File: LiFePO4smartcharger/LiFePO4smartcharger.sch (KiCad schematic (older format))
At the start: 106 parts, among them J1 Conn_01x02, J10 Conn_01x01, J11 Conn_01x01, J12 Conn_01x04, J14 Conn_01x02, J2 Conn_02x03_Odd_Even, J3 Conn_01x02, J4 Conn_01x02, J5 Conn_01x02, J6 Conn_01x01, J7 Conn_01x01, J8 Conn_01x02, J9 Conn_01x02, Q1 TIP42, Q2 TIP41, Q3 2N3906, Q4 TIP41C, U1 ATMEGA328P-PU, U2 LM358, U3 LCD-016N002L, U4 TL494, U5 LMT85, U9 LM7805_TO220, X3 16MHz

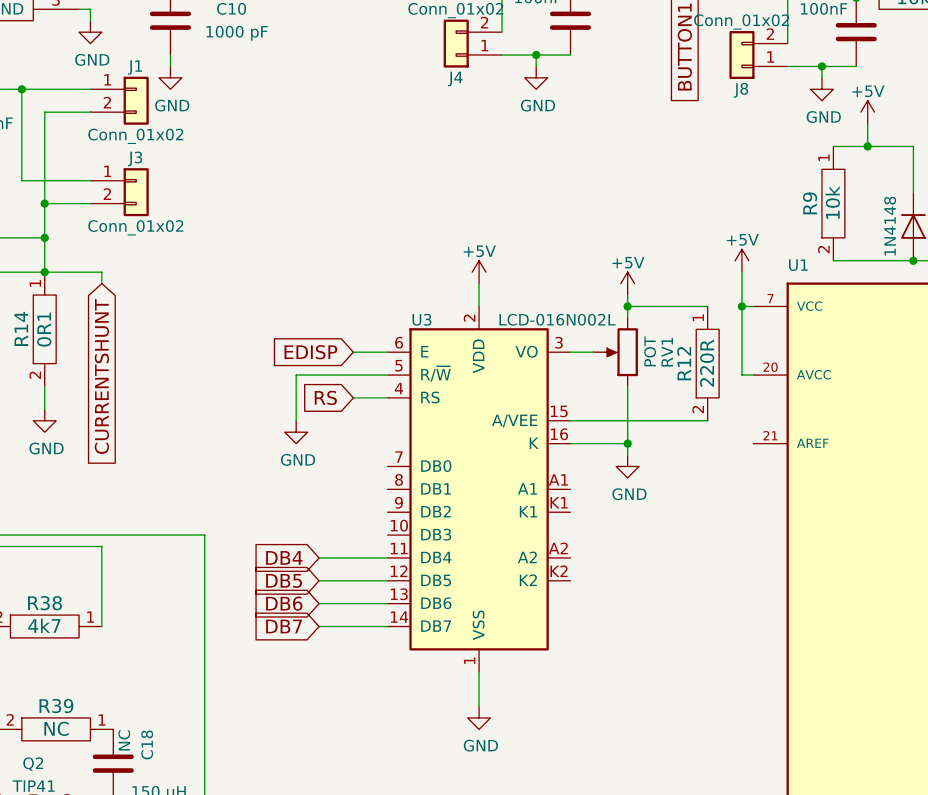
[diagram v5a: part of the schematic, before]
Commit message: Changed temperature sensor interface
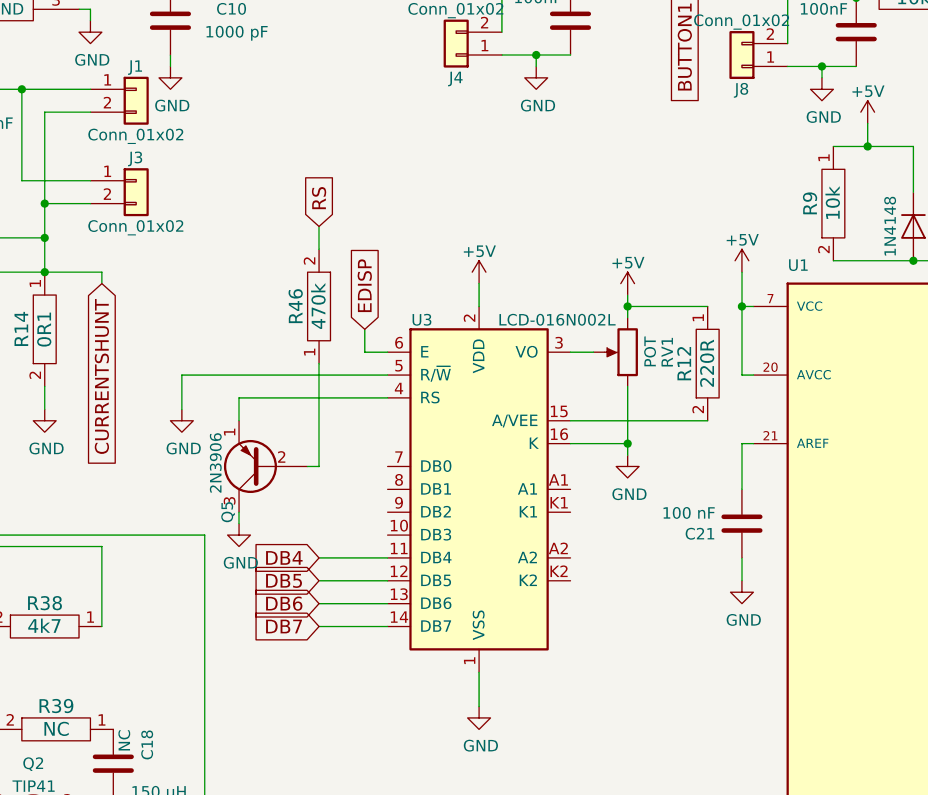
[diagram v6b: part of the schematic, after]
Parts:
- added C21: 100 nF, Capacitors_THT:C_Disc_D5.0mm_W2.5mm_P5.00mm, symbol C
- added Q5: 2N3906, TO_SOT_Packages_THT:TO-92_Inline_Wide, symbol 2N3906
- added R46: 470k, Resistors_THT:R_Axial_DIN0207_L6.3mm_D2.5mm_P7.62mm_Horizontal, symbol RES
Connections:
- net GND: now also C21.1, Q5.3 (C)
- net RS: now also R46.2; no longer U3.4 (RS)
- net at U1.21 (AREF): now also C21.2
- new net: Q5.1 (E), U3.4 (RS)
- new net: Q5.2 (B), R46.1
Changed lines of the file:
@@
 $EndComp
 $Comp
-L GND #PWR52
+L GND #PWR54
 U 1 1 572338B9
 P 10700 2000
-F 0 "#PWR52" H 10700 1750 50  0001 C CNN
+F 0 "#PWR54" H 10700 1750 50  0001 C CNN
 F 1 "GND" H 10708 1827 50  0000 C CNN
 F 2 "" H 10700 2000 50  0000 C CNN
@@
 $EndComp
 $Comp
-L GND #PWR56
+L GND #PWR58
 U 1 1 5B1253A7
 P 10950 3550
-F 0 "#PWR56" H 10950 3300 50  0001 C CNN
+F 0 "#PWR58" H 10950 3300 50  0001 C CNN
 F 1 "GND" H 10958 3377 50  0000 C CNN
 F 2 "" H 10950 3550 50  0000 C CNN
@@
 $EndComp
 $Comp
-L GND #PWR47
+L GND #PWR49
 U 1 1 5B126A05
 P 9800 2150
-F 0 "#PWR47" H 9800 1900 50  0001 C CNN
+F 0 "#PWR49" H 9800 1900 50  0001 C CNN
 F 1 "GND" H 9808 1977 50  0000 C CNN
 F 2 "" H 9800 2150 50  0000 C CNN
@@
 $EndComp
 $Comp
-L GND #PWR50
+L GND #PWR52
 U 1 1 5B0F2286
 P 10500 6200
-F 0 "#PWR50" H 10500 5950 50  0001 C CNN
+F 0 "#PWR52" H 10500 5950 50  0001 C CNN
 F 1 "GND" H 10508 6027 50  0000 C CNN
 F 2 "" H 10500 6200 50  0000 C CNN
@@
 $EndComp
 $Comp
-L GND #PWR55
+L GND #PWR57
 U 1 1 5B0F3459
 P 10900 6200
-F 0 "#PWR55" H 10900 5950 50  0001 C CNN
+F 0 "#PWR57" H 10900 5950 50  0001 C CNN
 F 1 "GND" H 10908 6027 50  0000 C CNN
 F 2 "" H 10900 6200 50  0000 C CNN
@@
 $EndComp
 $Comp
-L GND #PWR39
+L GND #PWR40
 U 1 1 5B1AAEE6
 P 7750 4900
-F 0 "#PWR39" H 7750 4650 50  0001 C CNN
+F 0 "#PWR40" H 7750 4650 50  0001 C CNN
 F 1 "GND" H 7900 4850 50  0000 C CNN
 F 2 "" H 7750 4900 50  0000 C CNN
@@
 $EndComp
 $Comp
-L GND #PWR53
+L GND #PWR55
 U 1 1 5B204A97
 P 10900 4400
-F 0 "#PWR53" H 10900 4150 50  0001 C CNN
+F 0 "#PWR55" H 10900 4150 50  0001 C CNN
 F 1 "GND" H 10908 4227 50  0000 C CNN
 F 2 "" H 10900 4400 50  0000 C CNN
@@
 $EndComp
 $Comp
-L +5V #PWR41
+L +5V #PWR42
 U 1 1 6041A1B7
 P 7800 2350
-F 0 "#PWR41" H 7800 2200 50  0001 C CNN
+F 0 "#PWR42" H 7800 2200 50  0001 C CNN
 F 1 "+5V" H 7800 2490 50  0000 C CNN
 F 2 "" H 7800 2350 50  0001 C CNN
@@
 $EndComp
 $Comp
-L +5V #PWR46
+L +5V #PWR48
 U 1 1 6041A8FB
 P 9750 1850
-F 0 "#PWR46" H 9750 1700 50  0001 C CNN
+F 0 "#PWR48" H 9750 1700 50  0001 C CNN
 F 1 "+5V" H 9750 1990 50  0000 C CNN
 F 2 "" H 9750 1850 50  0001 C CNN
@@
 $EndComp
 $Comp
-L GND #PWR48
+L GND #PWR50
 U 1 1 6041BB6E
 P 9800 6150
-F 0 "#PWR48" H 9800 5900 50  0001 C CNN
+F 0 "#PWR50" H 9800 5900 50  0001 C CNN
 F 1 "GND" H 9808 5977 50  0000 C CNN
 F 2 "" H 9800 6150 50  0000 C CNN
@@
 $EndComp
 $Comp
-L +5V #PWR54
+L +5V #PWR56
 U 1 1 6041BE51
 P 10900 5500
-F 0 "#PWR54" H 10900 5350 50  0001 C CNN
+F 0 "#PWR56" H 10900 5350 50  0001 C CNN
 F 1 "+5V" H 10900 5640 50  0000 C CNN
 F 2 "" H 10900 5500 50  0001 C CNN
@@
 $EndComp
 $Comp
-L +5V #PWR51
+L +5V #PWR53
 U 1 1 6041C537
 P 10700 1450
-F 0 "#PWR51" H 10700 1300 50  0001 C CNN
+F 0 "#PWR53" H 10700 1300 50  0001 C CNN
 F 1 "+5V" H 10700 1590 50  0000 C CNN
 F 2 "" H 10700 1450 50  0001 C CNN
@@
 $EndComp
 $Comp
-L +24V #PWR49
+L +24V #PWR51
 U 1 1 6041DB16
 P 9900 5700
-F 0 "#PWR49" H 9900 5550 50  0001 C CNN
+F 0 "#PWR51" H 9900 5550 50  0001 C CNN
 F 1 "+24V" H 9900 5840 50  0000 C CNN
 F 2 "" H 9900 5700 50  0001 C CNN
@@
 $EndComp
 $Comp
-L GND #PWR35
+L GND #PWR36
 U 1 1 6045525B
 P 6900 1450
-F 0 "#PWR35" H 6900 1200 50  0001 C CNN
+F 0 "#PWR36" H 6900 1200 50  0001 C CNN
 F 1 "GND" H 6908 1277 50  0000 C CNN
 F 2 "" H 6900 1450 50  0000 C CNN
@@
 $EndComp
 $Comp
-L +5V #PWR31
+L +5V #PWR32
 U 1 1 60457732
 P 6550 800
-F 0 "#PWR31" H 6550 650 50  0001 C CNN
+F 0 "#PWR32" H 6550 650 50  0001 C CNN
 F 1 "+5V" H 6550 940 50  0000 C CNN
 F 2 "" H 6550 800 50  0001 C CNN
@@
 $EndComp
 $Comp
-L GND #PWR42
+L GND #PWR44
 U 1 1 60459250
 P 8150 1500
-F 0 "#PWR42" H 8150 1250 50  0001 C CNN
+F 0 "#PWR44" H 8150 1250 50  0001 C CNN
 F 1 "GND" H 8158 1327 50  0000 C CNN
 F 2 "" H 8150 1500 50  0000 C CNN
@@
 $EndComp
 $Comp
-L +5V #PWR40
+L +5V #PWR41
 U 1 1 60459261
 P 7800 850
-F 0 "#PWR40" H 7800 700 50  0001 C CNN
+F 0 "#PWR41" H 7800 700 50  0001 C CNN
 F 1 "+5V" H 7800 990 50  0000 C CNN
 F 2 "" H 7800 850 50  0001 C CNN
@@
 $EndComp
 $Comp
-L GND #PWR45
+L GND #PWR47
 U 1 1 60459403
 P 9400 1450
-F 0 "#PWR45" H 9400 1200 50  0001 C CNN
+F 0 "#PWR47" H 9400 1200 50  0001 C CNN
 F 1 "GND" H 9408 1277 50  0000 C CNN
 F 2 "" H 9400 1450 50  0000 C CNN
@@
 $EndComp
 $Comp
-L +5V #PWR44
+L +5V #PWR46
 U 1 1 60459414
 P 9050 800
-F 0 "#PWR44" H 9050 650 50  0001 C CNN
+F 0 "#PWR46" H 9050 650 50  0001 C CNN
 F 1 "+5V" H 9050 940 50  0000 C CNN
 F 2 "" H 9050 800 50  0001 C CNN
@@
 A1
 $Comp
-L +5V #PWR32
+L +5V #PWR33
 U 1 1 6045AE76
 P 6650 2400
-F 0 "#PWR32" H 6650 2250 50  0001 C CNN
+F 0 "#PWR33" H 6650 2250 50  0001 C CNN
 F 1 "+5V" H 6650 2540 50  0000 C CNN
 F 2 "" H 6650 2400 50  0001 C CNN
@@
 $EndComp
 $Comp
-L GND #PWR33
+L GND #PWR34
 U 1 1 6045B46C
 P 6650 4250
-F 0 "#PWR33" H 6650 4000 50  0001 C CNN
+F 0 "#PWR34" H 6650 4000 50  0001 C CNN
 F 1 "GND" H 6658 4077 50  0000 C CNN
 F 2 "" H 6650 4250 50  0000 C CNN
@@
 $EndComp
 $Comp
-L +5V #PWR36
+L +5V #PWR37
 U 1 1 6045BD5D
 P 7300 2450
-F 0 "#PWR36" H 7300 2300 50  0001 C CNN
+F 0 "#PWR37" H 7300 2300 50  0001 C CNN
 F 1 "+5V" H 7300 2590 50  0000 C CNN
 F 2 "" H 7300 2450 50  0001 C CNN
@@
 $EndComp
 $Comp
-L GND #PWR37
+L GND #PWR38
 U 1 1 6045BFF2
 P 7300 3150
-F 0 "#PWR37" H 7300 2900 50  0001 C CNN
+F 0 "#PWR38" H 7300 2900 50  0001 C CNN
 F 1 "GND" H 7308 2977 50  0000 C CNN
 F 2 "" H 7300 3150 50  0000 C CNN
@@
 $EndComp
 $Comp
-L GND #PWR27
+L GND #PWR26
 U 1 1 6045D5DE
-P 5850 3000
-F 0 "#PWR27" H 5850 2750 50  0001 C CNN
-F 1 "GND" H 5858 2827 50  0000 C CNN
-F 2 "" H 5850 3000 50  0000 C CNN
-F 3 "" H 5850 3000 50  0000 C CNN
-	1    5850 3000
+P 5350 2950
+F 0 "#PWR26" H 5350 2700 50  0001 C CNN
+F 1 "GND" H 5358 2777 50  0000 C CNN
+F 2 "" H 5350 2950 50  0000 C CNN
+F 3 "" H 5350 2950 50  0000 C CNN
+	1    5350 2950
 	1    0    0    -1
 $EndComp
@@
 Text GLabel 5950 3900 0    60   Input ~ 0
 DB7
-Text GLabel 6100 2700 0    60   Input ~ 0
+Text GLabel 6150 2600 1    60   Input ~ 0
 EDISP
-Text GLabel 6100 2900 0    60   Input ~ 0
+Text GLabel 5950 2150 1    60   Input ~ 0
 RS
 $Comp
@@
 $EndComp
 $Comp
-L +5V #PWR43
+L +5V #PWR45
 U 1 1 6044A97E
 P 8350 1700
-F 0 "#PWR43" H 8350 1550 50  0001 C CNN
+F 0 "#PWR45" H 8350 1550 50  0001 C CNN
 F 1 "+5V" H 8350 1840 50  0000 C CNN
 F 2 "" H 8350 1700 50  0001 C CNN
@@
 $EndComp
 $Comp
-L GND #PWR28
+L GND #PWR29
 U 1 1 60459CB0
 P 6050 6950
-F 0 "#PWR28" H 6050 6700 50  0001 C CNN
+F 0 "#PWR29" H 6050 6700 50  0001 C CNN
 F 1 "GND" H 6058 6777 50  0000 C CNN
 F 2 "" H 6050 6950 50  0000 C CNN
@@
 $EndComp
 $Comp
-L GND #PWR30
+L GND #PWR31
 U 1 1 6047144E
 P 6500 6100
-F 0 "#PWR30" H 6500 5850 50  0001 C CNN
+F 0 "#PWR31" H 6500 5850 50  0001 C CNN
 F 1 "GND" H 6508 5927 50  0000 C CNN
 F 2 "" H 6500 6100 50  0000 C CNN
@@
 $EndComp
 $Comp
-L +5V #PWR34
+L +5V #PWR35
 U 1 1 60471C8D
 P 6850 4900
-F 0 "#PWR34" H 6850 4750 50  0001 C CNN
+F 0 "#PWR35" H 6850 4750 50  0001 C CNN
 F 1 "+5V" H 6850 5040 50  0000 C CNN
 F 2 "" H 6850 4900 50  0001 C CNN
@@
 $EndComp
 $Comp
-L GND #PWR38
+L GND #PWR39
 U 1 1 60492DFA
 P 7300 5300
-F 0 "#PWR38" H 7300 5050 50  0001 C CNN
+F 0 "#PWR39" H 7300 5050 50  0001 C CNN
 F 1 "GND" H 7308 5127 50  0000 C CNN
 F 2 "" H 7300 5300 50  0000 C CNN
@@
 $EndComp
 $Comp
-L GND #PWR29
+L GND #PWR30
 U 1 1 6057337F
 P 6200 6100
-F 0 "#PWR29" H 6200 5850 50  0001 C CNN
+F 0 "#PWR30" H 6200 5850 50  0001 C CNN
 F 1 "GND" H 6208 5927 50  0000 C CNN
 F 2 "" H 6200 6100 50  0000 C CNN
@@
 $EndComp
 $Comp
-L GND #PWR26
+L GND #PWR27
 U 1 1 605AC029
 P 5500 7100
-F 0 "#PWR26" H 5500 6850 50  0001 C CNN
+F 0 "#PWR27" H 5500 6850 50  0001 C CNN
 F 1 "GND" H 5508 6927 50  0000 C CNN
 F 2 "" H 5500 7100 50  0000 C CNN
@@
 Connection ~ 7300 3100
 Wire Wire Line
-	5850 2800 6250 2800
+	5350 2800 6250 2800
 Wire Wire Line
 	9550 1100 9250 1100
@@
 	6250 3900 5950 3900
 Wire Wire Line
-	6250 2700 6100 2700
-Wire Wire Line
-	6100 2900 6250 2900
-Wire Wire Line
-	5850 3000 5850 2800
+	5600 2900 6250 2900
 Wire Wire Line
 	7650 2500 7300 2500
@@
 Text GLabel 5850 1050 2    60   Input ~ 0
 RS
+Wire Wire Line
+	5350 2800 5350 2950
+Wire Wire Line
+	6150 2600 6150 2700
+Wire Wire Line
+	6150 2700 6250 2700
+$Comp
+L 2N3906 Q5
+U 1 1 630F292D
+P 5700 3200
+F 0 "Q5" V 5850 3350 50  0000 L CNN
+F 1 "2N3906" V 5900 3050 50  0000 L CNN
+F 2 "TO_SOT_Packages_THT:TO-92_Inline_Wide" H 5900 3125 50  0001 L CIN
+F 3 "" H 5700 3200 50  0001 L CNN
+	1    5700 3200
+	-1   0    0    1
+$EndComp
+$Comp
+L RES R46
+U 1 1 630F3A95
+P 5950 2500
+F 0 "R46" H 5950 2400 60  0000 C CNN
+F 1 "470k" H 5950 2500 60  0000 C CNN
+F 2 "Resistors_THT:R_Axial_DIN0207_L6.3mm_D2.5mm_P7.62mm_Horizontal" H 5900 2500 60  0001 C CNN
+F 3 "" H 5900 2500 60  0000 C CNN
+	1    5950 2500
+	0    1    1    0
+$EndComp
+$Comp
+L GND #PWR28
+U 1 1 630F4421
+P 5600 3450
+F 0 "#PWR28" H 5600 3200 50  0001 C CNN
+F 1 "GND" H 5608 3277 50  0000 C CNN
+F 2 "" H 5600 3450 50  0000 C CNN
+F 3 "" H 5600 3450 50  0000 C CNN
+	1    5600 3450
+	1    0    0    -1
+$EndComp
+Wire Wire Line
+	5600 3450 5600 3400
+Wire Wire Line
+	5600 3000 5600 2900
+Wire Wire Line
+	5950 2750 5950 3200
+Wire Wire Line
+	5950 3200 5900 3200
+Wire Wire Line
+	5950 2150 5950 2250
+$Comp
+L C C21
+U 1 1 630F6BB6
+P 7800 3450
+F 0 "C21" H 7915 3496 50  0000 L CNN
+F 1 "100 nF" H 7915 3405 50  0000 L CNN
+F 2 "Capacitors_THT:C_Disc_D5.0mm_W2.5mm_P5.00mm" H 7838 3300 50  0001 C CNN
+F 3 "" H 7800 3450 50  0000 C CNN
+	1    7800 3450
+	-1   0    0    1
+$EndComp
+Wire Wire Line
+	7800 3300 7800 3100
+Wire Wire Line
+	7800 3100 7850 3100
+$Comp
+L GND #PWR43
+U 1 1 630F6F9E
+P 7800 3700
+F 0 "#PWR43" H 7800 3450 50  0001 C CNN
+F 1 "GND" H 7808 3527 50  0000 C CNN
+F 2 "" H 7800 3700 50  0000 C CNN
+F 3 "" H 7800 3700 50  0000 C CNN
+	1    7800 3700
+	1    0    0    -1
+$EndComp
+Wire Wire Line
+	7800 3700 7800 3600
 $EndSCHEMATC

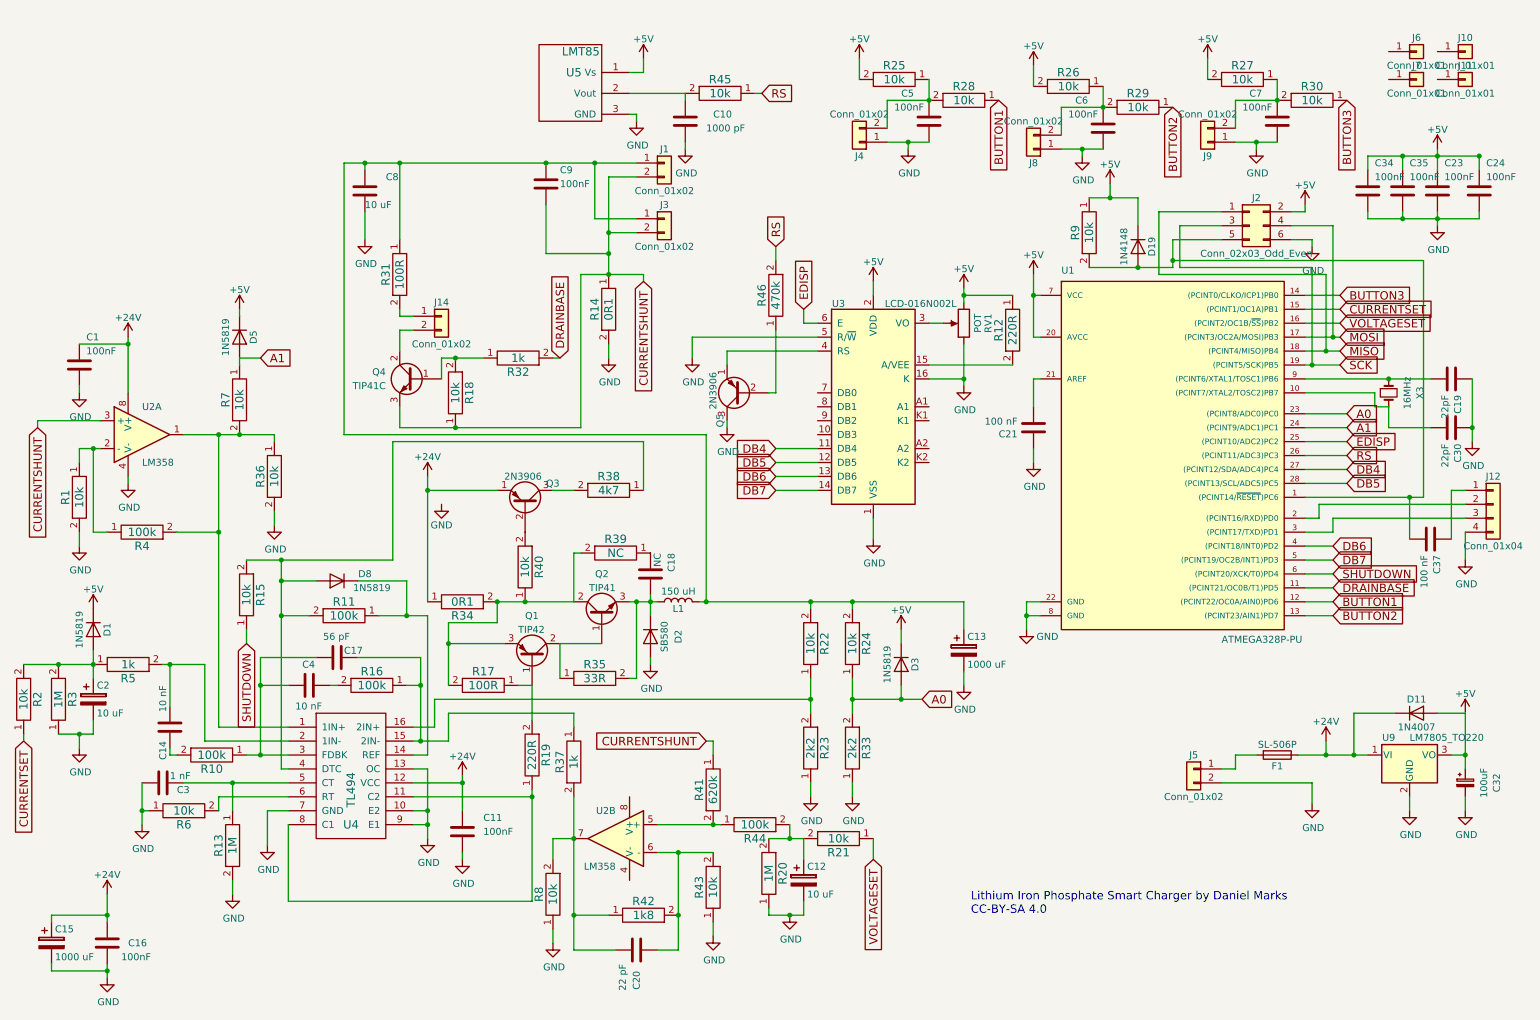
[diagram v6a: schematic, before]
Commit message: Changed to use 5 buttons
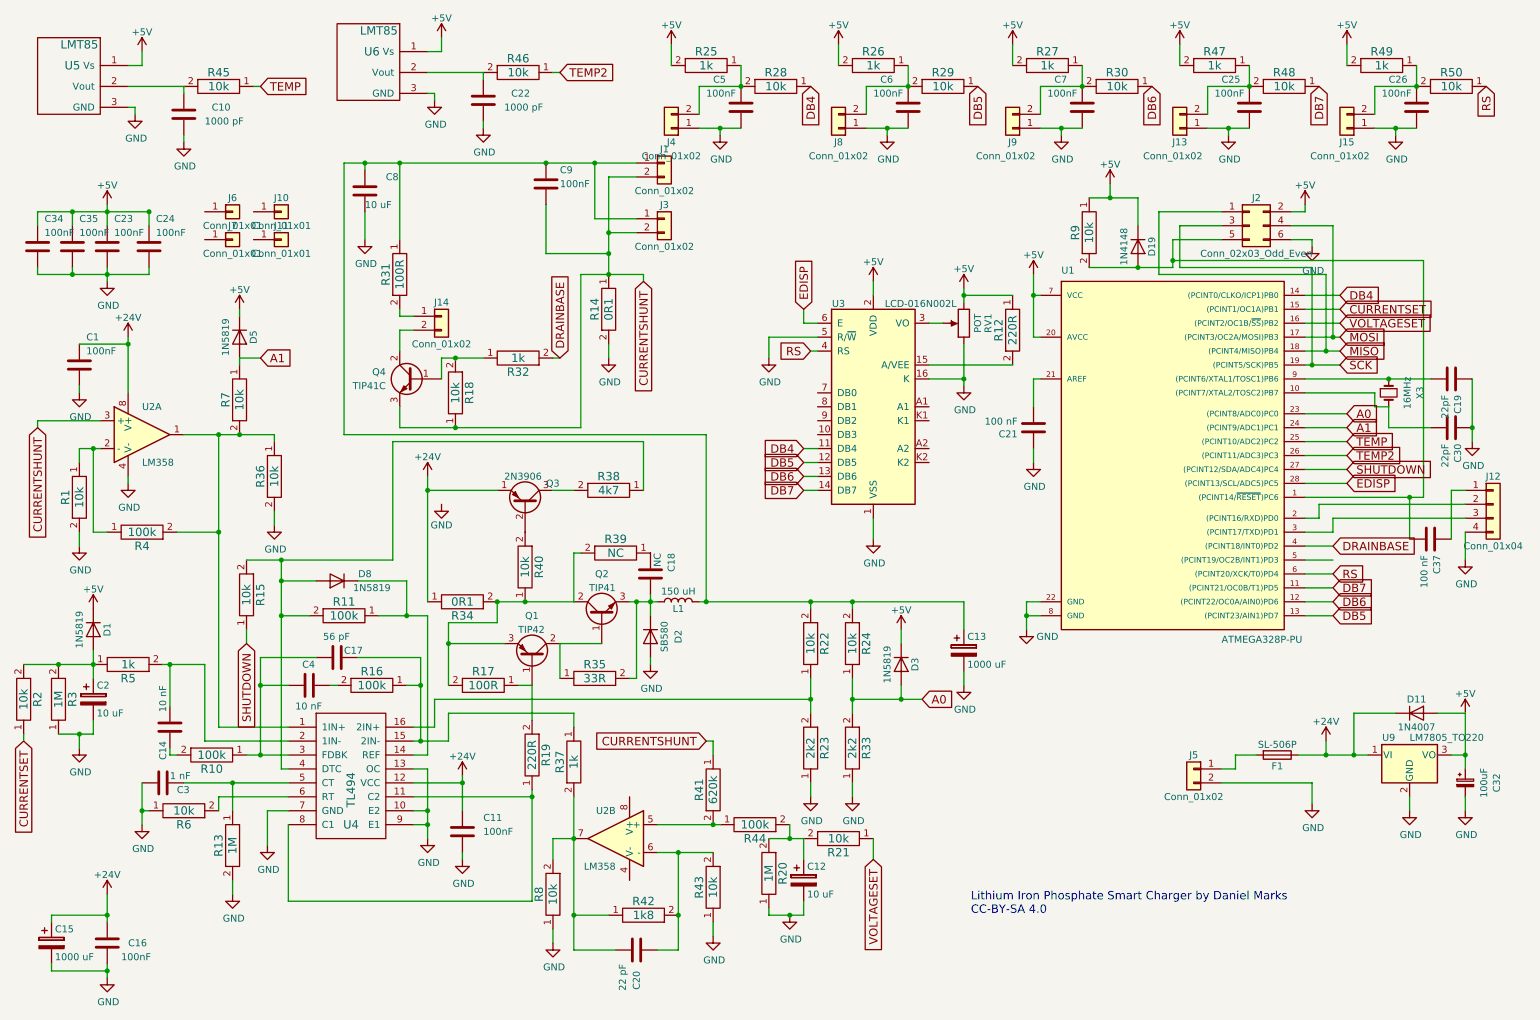
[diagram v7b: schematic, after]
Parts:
- removed Q5: 2N3906, TO_SOT_Packages_THT:TO-92_Inline_Wide, symbol 2N3906
- added C22: 1000 pF, Capacitors_THT:C_Disc_D5.0mm_W2.5mm_P5.00mm, symbol C
- added C25, C26: 100nF, Capacitors_THT:C_Disc_D5.0mm_W2.5mm_P5.00mm, symbol C
- added J13, J15: Conn_01x02, Buttons_Switches_THT:SW_PUSH_6mm_h4.3mm, symbol Conn_01x02
- added R47, R49: 1k, Resistors_THT:R_Axial_DIN0207_L6.3mm_D2.5mm_P7.62mm_Horizontal, symbol RES
- added R48, R50: 10k, Resistors_THT:R_Axial_DIN0207_L6.3mm_D2.5mm_P7.62mm_Horizontal, symbol RES
- added U6: LMT85, TO_SOT_Packages_THT:TO-92_Inline_Wide, symbol LM35
- R25, R26, R27: value 10k -> 1k
- R46: value 470k -> 10k
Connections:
- net BUTTON2 is gone; now on net DB5: R29.1, U1.13 ((PCINT23/AIN1)PD7)
- net +5V: now also R47.2, R49.2, U6.1 (Vs)
- net DB4: now also R28.1, U1.14 ((PCINT0/CLKO/ICP1)PB0); no longer U1.27 ((PCINT12/SDA/ADC4)PC4)
- net DB5: no longer U1.28 ((PCINT13/SCL/ADC5)PC5)
- net DB6: now also R30.1, U1.12 ((PCINT22/OC0A/AIN0)PD6); no longer U1.4 ((PCINT18/INT0)PD2)
- net DB7: now also U1.11 ((PCINT21/OC0B/T1)PD5), R48.1; no longer U1.5 ((PCINT19/OC2B/INT1)PD3)
- net DRAINBASE: now also U1.4 ((PCINT18/INT0)PD2); no longer U1.11 ((PCINT21/OC0B/T1)PD5)
- net EDISP: now also U1.28 ((PCINT13/SCL/ADC5)PC5); no longer U1.25 ((PCINT10/ADC2)PC2)
- net GND: now also C22.2, C25.2, C26.2, J13.1 (Pin_1), J15.1 (Pin_1), U6.3 (GND)
- net RS: now also U1.6 ((PCINT20/XCK/T0)PD4), U3.4 (RS), R50.1; no longer R45.1, R46.2, U1.26 ((PCINT11/ADC3)PC3)
- net SHUTDOWN: now also U1.27 ((PCINT12/SDA/ADC4)PC4); no longer U1.6 ((PCINT20/XCK/T0)PD4)
- net TEMP2: now reaches R46.1
- net TEMP2: now also U1.26 ((PCINT11/ADC3)PC3)
- removed net BUTTON1: R28.1, U1.12 ((PCINT22/OC0A/AIN0)PD6)
- removed net BUTTON3: R30.1, U1.14 ((PCINT0/CLKO/ICP1)PB0)
- new net: C25.1, J13.2 (Pin_2), R47.1, R48.2
- new net: C26.1, J15.2 (Pin_2), R49.1, R50.2
- new net: C22.1, R46.2, U6.2 (Vout)
- new net TEMP: R45.1, U1.25 ((PCINT10/ADC2)PC2)
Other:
- moved on the sheet: C10, C23, C24, C34, C35, C5, C6, C7, J10, J11, J4, J6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
